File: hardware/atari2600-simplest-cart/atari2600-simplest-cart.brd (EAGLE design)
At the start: 40 x 53.6 mm, 4 parts, among them CON1 24PINEDGE-ATARI-2600, IC3 74S04N

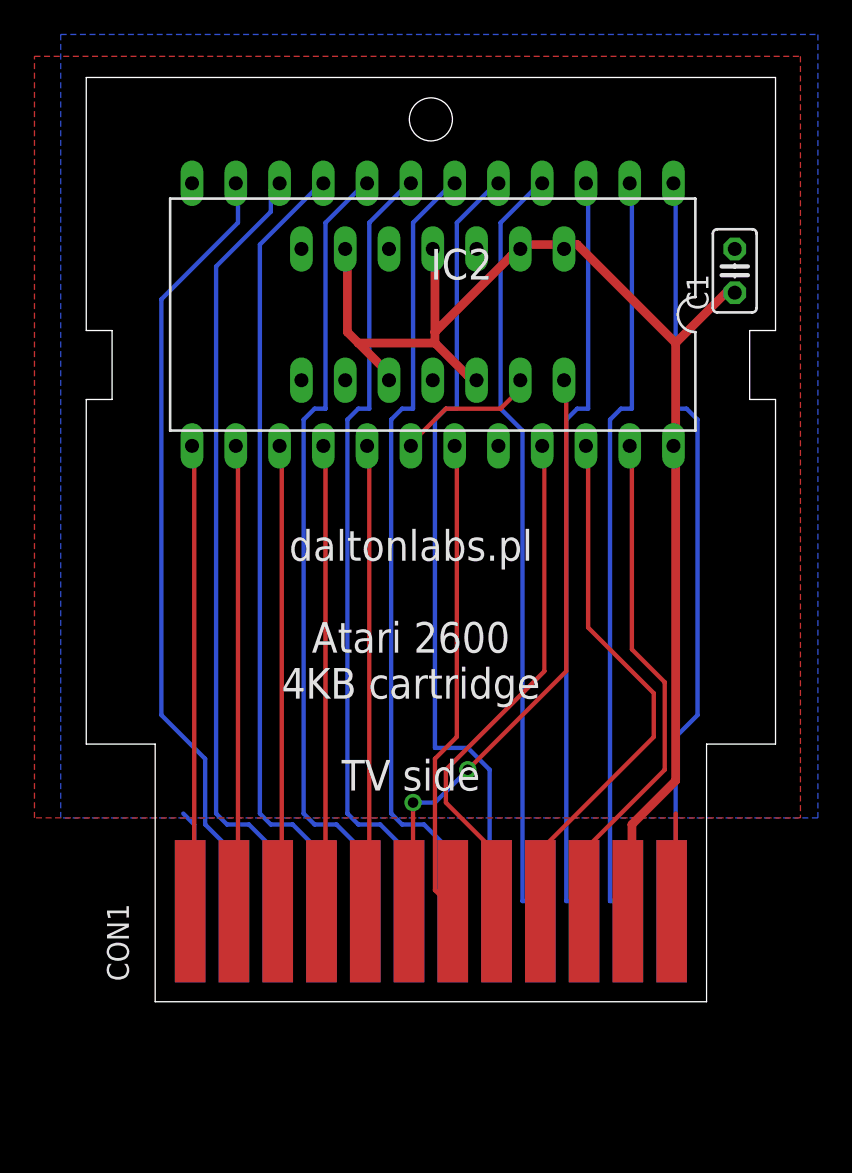
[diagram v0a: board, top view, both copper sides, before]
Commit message: Replace IC inverter with transistor based inverter on PCB
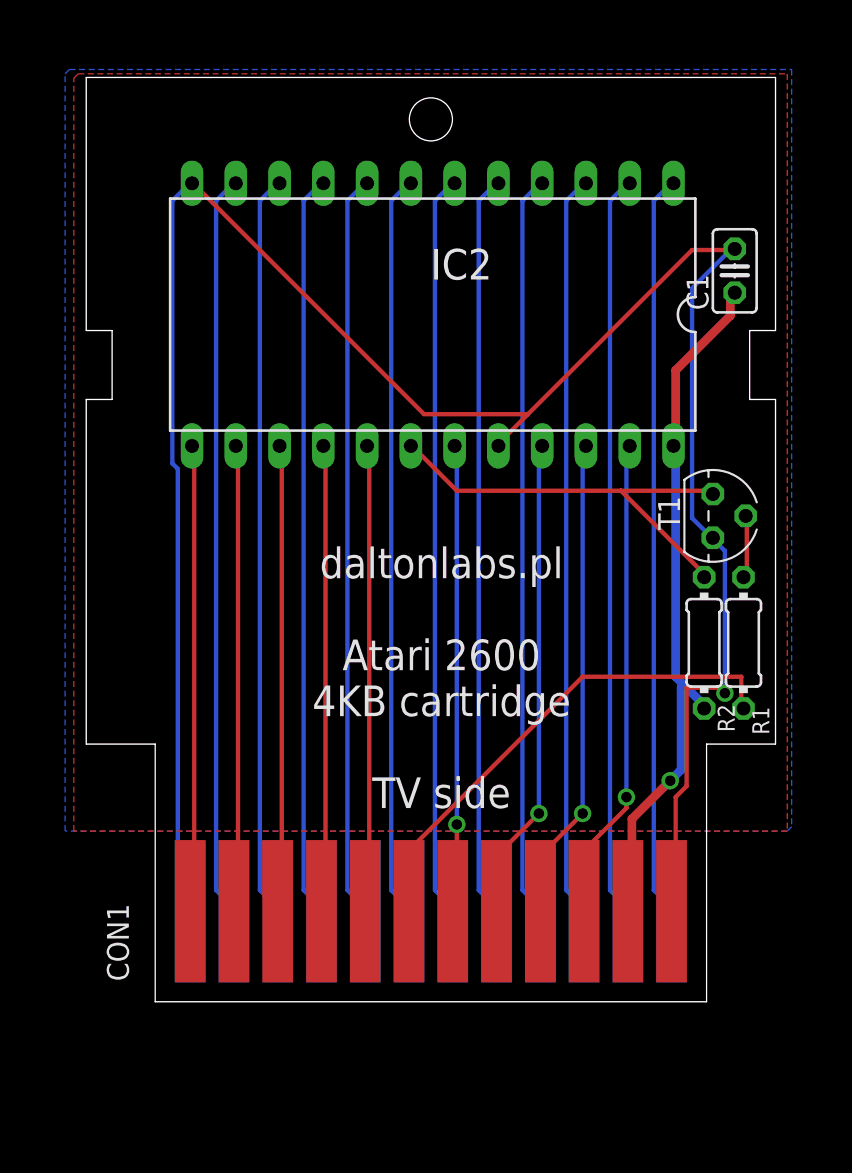
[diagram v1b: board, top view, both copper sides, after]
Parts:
- removed IC3: 74S04N, 74xx-eu:DIL14
- added R1: 10k, rcl:0204/7
- added R2: 1k, rcl:0204/7
- added T1: BC337, transistor:TO92
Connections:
- new net N$2: R1.2, T1.2
- net A12: now also R1.1; no longer IC3.1
- net A12INV: now also R2.1, T1.3; no longer IC3.2
- net GND: now also T1.1; no longer IC3.7
- net VCC: now also R2.2; no longer IC3.11, IC3.13, IC3.14, IC3.3, IC3.5, IC3.9
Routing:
- net GND: track 11.7 -> 130.1 mm, vias 0 -> 1
- net VCC: track 79.6 -> 40.9 mm, vias 0 -> 1
- net A12INV: track 8.35 -> 25.7 mm
- net A12: track 35.3 -> 28.8 mm, vias 2 -> 0
- net N$2: track 0.00 -> 3.63 mm
- net A3: track 46.7 -> 43.2 mm
- net A2: track 46.4 -> 43.2 mm
- net A1: track 46.4 -> 43.2 mm
- net A0: track 46.4 -> 43.2 mm
- net A9: track 31.3 -> 28.1 mm, vias 0 -> 1
- net O0: track 46.0 -> 43.2 mm
- net O1: track 46.0 -> 43.2 mm
- net O2: track 45.8 -> 43.2 mm
- net A11: track 30.6 -> 28.1 mm, vias 0 -> 1
- net A8: track 29.7 -> 28.1 mm, vias 0 -> 1
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
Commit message: Add missing capacitor to the cartridge board schematic
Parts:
- added C2: 1nF, rcl:C025-025X050
- R1: value 10k -> 3k3
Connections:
- net A12: now also C2.2
- net N$2: now also C2.1
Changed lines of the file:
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@@
 <attribute name="VALUE" x="53.594" y="28.067" size="1.27" layer="27" ratio="10" rot="R270"/>
 </element>
-<element name="R1" library="rcl" library_urn="urn:adsk.eagle:library:334" package="0204/7" package3d_urn="urn:adsk.eagle:package:23498/2" value="10k" x="56.642" y="23.876" smashed="yes" rot="R90">
+<element name="R1" library="rcl" library_urn="urn:adsk.eagle:library:334" package="0204/7" package3d_urn="urn:adsk.eagle:package:23498/2" value="3k3" x="56.642" y="23.876" smashed="yes" rot="R90">
 <attribute name="NAME" x="58.1406" y="18.542" size="0.9906" layer="25" ratio="10" rot="R90"/>
 <attribute name="POPULARITY" value="79" x="56.642" y="23.876" size="1.778" layer="27" rot="R90" display="off"/>
@@
 <attribute name="SPICEPREFIX" value="R" x="54.356" y="23.876" size="1.778" layer="27" rot="R270" display="off"/>
 <attribute name="VALUE" x="53.8734" y="25.5016" size="0.9906" layer="27" ratio="10" rot="R270"/>
+</element>
+<element name="C2" library="rcl" library_urn="urn:adsk.eagle:library:334" package="C025-025X050" package3d_urn="urn:adsk.eagle:package:23629/2" value="1nF" x="20.066" y="-3.556" smashed="yes">
+<attribute name="NAME" x="17.78" y="-2.032" size="1.27" layer="25" ratio="10"/>
+<attribute name="POPULARITY" value="65" x="20.066" y="-3.556" size="1.778" layer="27" display="off"/>
+<attribute name="SPICEPREFIX" value="C" x="20.066" y="-3.556" size="1.778" layer="27" display="off"/>
+<attribute name="VALUE" x="17.78" y="-6.35" size="1.27" layer="27" ratio="10"/>
 </element>
 </elements>
@@
 <wire x1="56.515" y1="20.32" x2="56.642" y2="20.066" width="0.254" layer="1"/>
 <wire x1="37.465" y1="8.5725" x2="37.23" y2="8.302" width="0.254" layer="1"/>
+<contactref element="C2" pad="2"/>
+<wire x1="21.336" y1="-3.556" x2="37.23" y2="8.302" width="0" layer="19" extent="1-1"/>
 </signal>
 <signal name="A12INV">
@@
 <wire x1="56.8325" y1="27.94" x2="56.642" y2="27.686" width="0.254" layer="1"/>
 <wire x1="56.8325" y1="31.115" x2="56.769" y2="31.242" width="0.254" layer="1"/>
+<contactref element="C2" pad="1"/>
+<wire x1="18.796" y1="-3.556" x2="56.642" y2="27.686" width="0" layer="19" extent="1-1"/>
 </signal>
 </signals>

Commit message: Add missing capacitor to the cartridge board PCB
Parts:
- moved C2 45.9 mm to (56.6, 24.1), flipped to the bottom, turned to 270 degrees
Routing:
- net N$2: track 3.63 -> 6.68 mm
- net A12: track 28.8 -> 29.9 mm
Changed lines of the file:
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@@
 <attribute name="VALUE" x="53.8734" y="25.5016" size="0.9906" layer="27" ratio="10" rot="R270"/>
 </element>
-<element name="C2" library="rcl" library_urn="urn:adsk.eagle:library:334" package="C025-025X050" package3d_urn="urn:adsk.eagle:package:23629/2" value="1nF" x="20.066" y="-3.556" smashed="yes">
-<attribute name="NAME" x="17.78" y="-2.032" size="1.27" layer="25" ratio="10"/>
-<attribute name="POPULARITY" value="65" x="20.066" y="-3.556" size="1.778" layer="27" display="off"/>
-<attribute name="SPICEPREFIX" value="C" x="20.066" y="-3.556" size="1.778" layer="27" display="off"/>
-<attribute name="VALUE" x="17.78" y="-6.35" size="1.27" layer="27" ratio="10"/>
+<element name="C2" library="rcl" library_urn="urn:adsk.eagle:library:334" package="C025-025X050" package3d_urn="urn:adsk.eagle:package:23629/2" value="1nF" x="56.642" y="24.13" smashed="yes" rot="MR270">
+<attribute name="NAME" x="55.118" y="26.416" size="1.27" layer="26" ratio="10" rot="MR270"/>
+<attribute name="POPULARITY" value="65" x="56.642" y="24.13" size="1.778" layer="28" rot="MR270" display="off"/>
+<attribute name="SPICEPREFIX" value="C" x="56.642" y="24.13" size="1.778" layer="28" rot="MR270" display="off"/>
+<attribute name="VALUE" x="59.436" y="26.416" size="1.27" layer="28" ratio="10" rot="MR270"/>
 </element>
 </elements>
@@
 <contactref element="CON1" pad="6"/>
 <contactref element="R1" pad="1"/>
-<wire x1="56.515" y1="21.9075" x2="56.515" y2="20.32" width="0.254" layer="1"/>
+<wire x1="56.515" y1="21.9075" x2="56.515" y2="21.59" width="0.254" layer="1"/>
+<wire x1="56.515" y1="21.59" x2="56.515" y2="20.32" width="0.254" layer="1"/>
 <wire x1="47.3075" y1="21.9075" x2="56.515" y2="21.9075" width="0.254" layer="1"/>
 <wire x1="37.465" y1="12.065" x2="47.3075" y2="21.9075" width="0.254" layer="1"/>
@@
 <wire x1="37.465" y1="8.5725" x2="37.23" y2="8.302" width="0.254" layer="1"/>
 <contactref element="C2" pad="2"/>
-<wire x1="21.336" y1="-3.556" x2="37.23" y2="8.302" width="0" layer="19" extent="1-1"/>
+<wire x1="56.515" y1="21.9075" x2="56.515" y2="22.86" width="0.254" layer="1"/>
+<wire x1="56.515" y1="22.86" x2="56.642" y2="22.86" width="0.254" layer="1"/>
 </signal>
 <signal name="A12INV">
@@
 <wire x1="56.8325" y1="31.115" x2="56.769" y2="31.242" width="0.254" layer="1"/>
 <contactref element="C2" pad="1"/>
-<wire x1="18.796" y1="-3.556" x2="56.642" y2="27.686" width="0" layer="19" extent="1-1"/>
+<wire x1="57.15" y1="27.305" x2="57.15" y2="25.4" width="0.254" layer="1"/>
+<wire x1="57.15" y1="25.4" x2="56.642" y2="25.4" width="0.254" layer="1"/>
+<wire x1="57.15" y1="27.305" x2="56.642" y2="27.686" width="0.254" layer="1"/>
 </signal>
 </signals>
